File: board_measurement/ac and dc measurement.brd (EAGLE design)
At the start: 100 x 80 mm, 40 parts, among them J1 22-27-2041-04, Q1 BUZ10

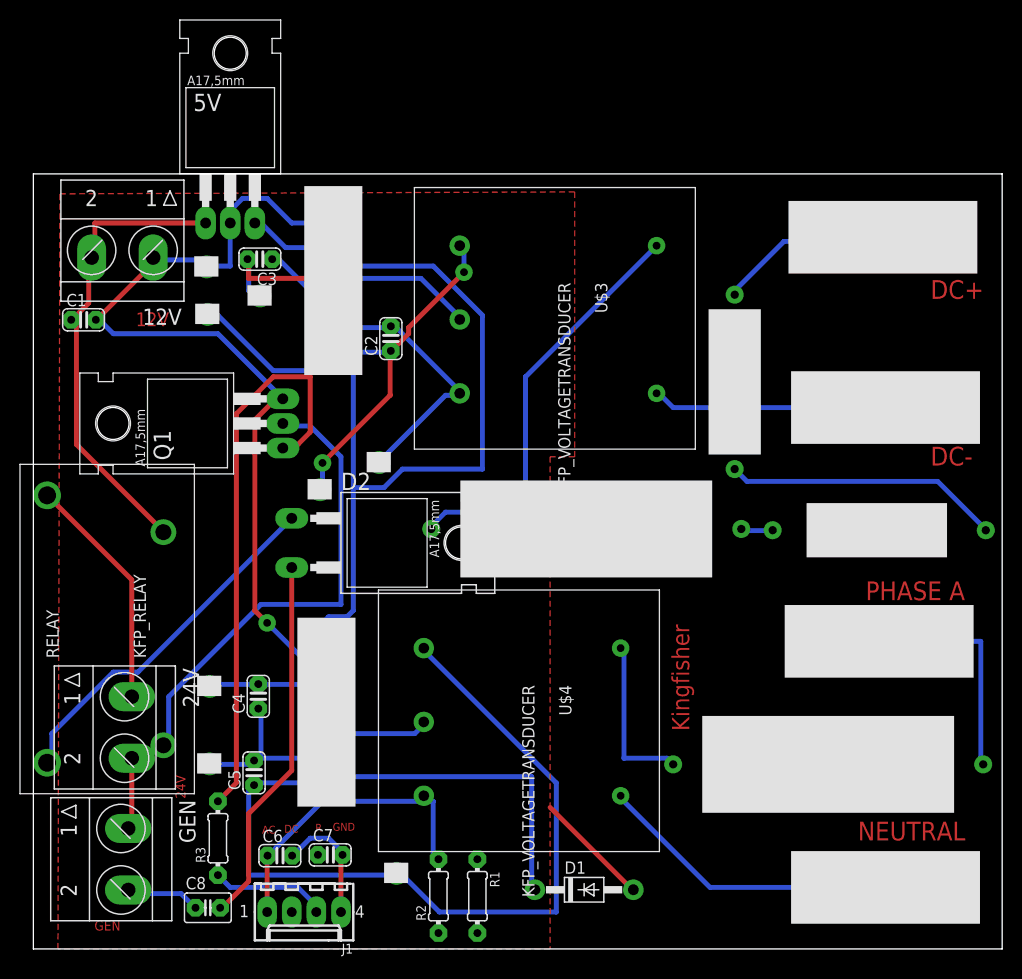
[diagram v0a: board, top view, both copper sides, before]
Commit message: measurement and exitation added, all boards labeled for manufacturing
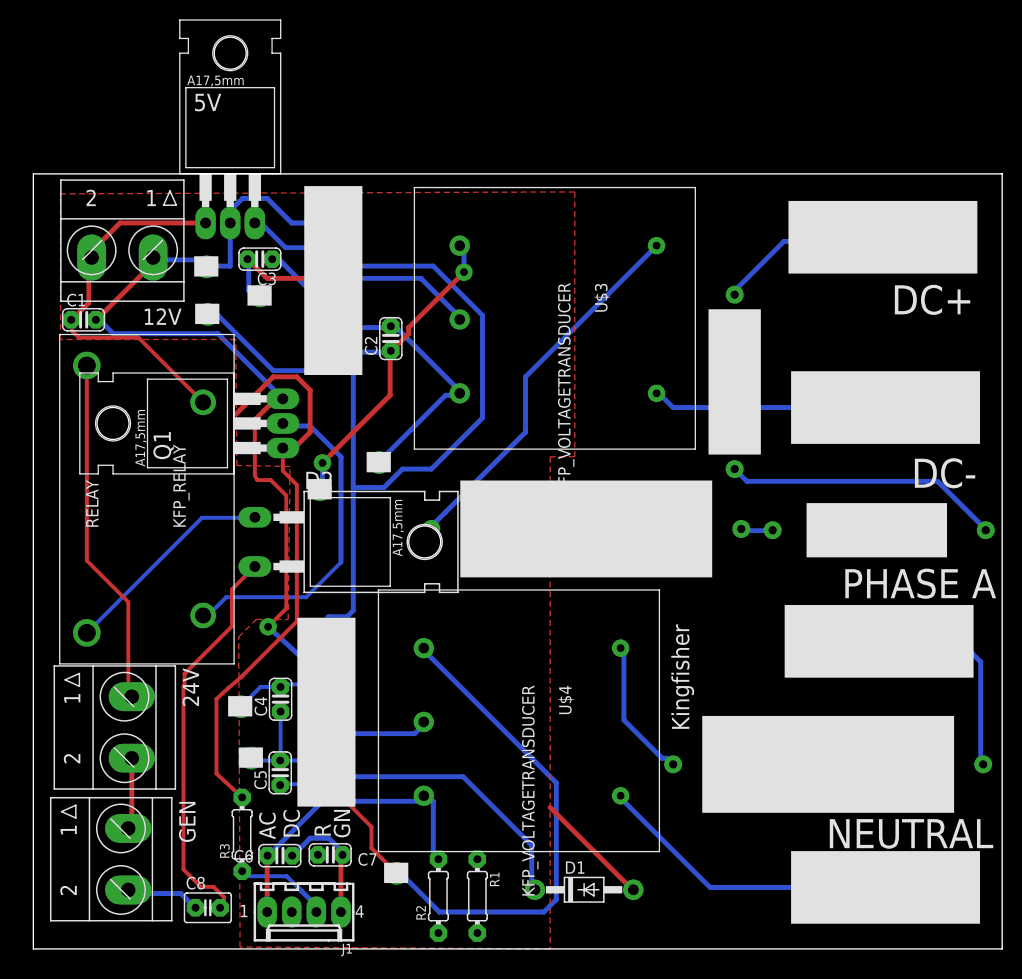
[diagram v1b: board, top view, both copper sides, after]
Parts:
- moved RELAY 14.0 mm to (11.7, 46.4)
- moved U$20 4.34 mm to (22.5, 19.7)
- moved U$18 3.83 mm to (21.4, 25.0)
- moved D2 3.80 mm to (29.2, 42.0)
- moved C5 2.70 mm to (25.5, 18.2)
- moved R3 2.53 mm to (21.6, 11.8)
- moved C4 2.32 mm to (25.5, 25.8)
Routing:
- net N$26: track 37.2 -> 22.3 mm
- net N$14: track 49.6 -> 34.8 mm
- net N$8: track 81.8 -> 68.3 mm, vias 0 -> 1
- net N$27: track 24.4 -> 36.1 mm
- net N$7: track 52.5 -> 42.9 mm
- net N$25: track 48.5 -> 39.5 mm
- net N$12: track 43.7 -> 38.8 mm
- net N$2: track 110.5 -> 107.4 mm
- net N$20: track 38.3 -> 41.0 mm
- net N$1: track 88.2 -> 90.6 mm
- net N$4: track 27.9 -> 25.6 mm
- net N$10: track 16.8 -> 14.5 mm
- net N$24: track 12.1 -> 10.3 mm
- net N$15: track 28.2 -> 26.9 mm
- net N$3: track 30.4 -> 29.3 mm
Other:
- board text added: "57183-C"
- board text removed: "12V"
- board text removed: "24V"
- board text removed: "GEN"
